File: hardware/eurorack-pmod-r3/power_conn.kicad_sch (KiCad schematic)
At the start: 24 parts, among them J1 CONN 2x5 P=2.54mm, J2 CONN 2x6 P=2.54mm

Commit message: Place everything on board, fix some bugs
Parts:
- removed C15, C5, C6: 47uF, Capacitor_SMD:CP_Elec_6.3x5.4, symbol Device:C_Polarized_Small
- added C13: 47.0uF, Capacitor_Tantalum_SMD:CP_EIA-3216-10_Kemet-I, symbol Device:C_Polarized_Small
- added J3: Conn_01x14_Socket, Connector_FFC-FPC:Hirose_FH12-14S-0.5SH_1x14-1MP_P0.50mm_Horizontal, symbol Connector:Conn_01x14_Socket
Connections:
- net BICK: now also J3.10 (Pin_10)
- net GND: now also J3.5 (Pin_5)
- net GNDD: now also C13.2, J3.6 (Pin_6)
- net LRCK: now also J3.9 (Pin_9)
- net MCLK: now also J3.11 (Pin_11)
- net PDN: now also J3.12 (Pin_12)
- net SCL: now also J3.14 (Pin_14)
- net SDA: now also J3.13 (Pin_13)
- net SDIN1: now also J3.7 (Pin_7)
- net SDOUT1: now also J3.8 (Pin_8)
- net VDD: now also C13.1
- net C_P12V: now reaches D1.1 (K), L1.2
- net C_P12V: now also J3.3 (Pin_3)
- net C_N12V: now reaches D2.2 (A), L2.2
- net C_N12V: now also J3.1 (Pin_1)
- no-connect marks 0 -> 2
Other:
- note added: "FFC INGRESS"
- note added: "[REMOVED] Daughterboard AUX"
- note removed: "[REMOVED] DAUGHTERBOARD AUX"
- moved on the sheet: D1, D2, J1, L1, L2

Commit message: Almost ready for layout
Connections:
- net +12V: now also J3.3 (Pin_3)
- net -12V: now also J3.1 (Pin_1)
- net GND: now also J3.4 (Pin_4); no longer J3.5 (Pin_5)
- net VDD: now also J3.5 (Pin_5)
- net C_N12V: no longer names the net of D2.2 (A), L2.2
- net C_N12V: no longer J3.1 (Pin_1)
- net C_P12V: no longer names the net of D1.1 (K), L1.2
- net C_P12V: no longer J3.3 (Pin_3)
- no-connect marks 2 -> 1
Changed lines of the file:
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@@
   (junction (at 45.72 88.9) (diameter 0) (color 0 0 0 0)
   )
-  (junction (at 50.038 43.18) (diameter 0) (color 0 0 0 0)
-  )
   (junction (at 96.012 30.099) (diameter 0) (color 0 0 0 0)
   )
@@
   (junction (at 25.4 38.1) (diameter 0) (color 0 0 0 0)
   )
-  (junction (at 50.038 33.02) (diameter 0) (color 0 0 0 0)
-  )
   (junction (at 77.089 50.292) (diameter 0) (color 0 0 0 0)
   )
@@
   (junction (at 102.235 94.615) (diameter 0) (color 0 0 0 0)
   )
-  (no_connect (at 148.844 46.228))
   (no_connect (at 148.844 41.148))
   (wire (pts (xy 75.184 45.212) (xy 77.089 45.212))
@@
     (stroke (width 0) (type default))
   )
-  (wire (pts (xy 50.038 43.18) (xy 52.705 43.18))
+  (wire (pts (xy 49.53 43.18) (xy 52.705 43.18))
     (stroke (width 0) (type default))
   )
@@
     (stroke (width 0) (type default))
   )
-  (wire (pts (xy 137.16 46.99) (xy 137.16 48.768))
-    (stroke (width 0) (type default))
-  )
   (wire (pts (xy 33.02 88.9) (xy 33.02 91.44))
     (stroke (width 0) (type default))
@@
     (stroke (width 0) (type default))
   )
-  (wire (pts (xy 49.53 33.02) (xy 50.038 33.02))
-    (stroke (width 0) (type default))
-  )
   (wire (pts (xy 136.144 51.308) (xy 148.844 51.308))
     (stroke (width 0) (type default))
@@
     (stroke (width 0) (type default))
   )
-  (wire (pts (xy 50.038 32.258) (xy 50.038 33.02))
-    (stroke (width 0) (type default))
-  )
   (wire (pts (xy 39.37 40.64) (xy 40.64 40.64))
     (stroke (width 0) (type default))
@@
     (stroke (width 0) (type default))
   )
-  (wire (pts (xy 50.038 42.418) (xy 50.038 43.18))
+  (wire (pts (xy 135.636 46.228) (xy 148.844 46.228))
     (stroke (width 0) (type default))
   )
@@
     (stroke (width 0) (type default))
   )
-  (wire (pts (xy 137.16 48.768) (xy 148.844 48.768))
-    (stroke (width 0) (type default))
-  )
   (wire (pts (xy 93.345 73.279) (xy 95.885 73.279))
     (stroke (width 0) (type default))
@@
     (stroke (width 0) (type default))
   )
-  (wire (pts (xy 50.038 33.02) (xy 52.705 33.02))
+  (wire (pts (xy 49.53 33.02) (xy 52.705 33.02))
     (stroke (width 0) (type default))
   )
@@
     (stroke (width 0) (type default))
   )
-  (wire (pts (xy 136.398 46.99) (xy 137.16 46.99))
-    (stroke (width 0) (type default))
-  )
   (wire (pts (xy 25.4 38.1) (xy 26.67 38.1))
     (stroke (width 0) (type default))
@@
     (stroke (width 0) (type default))
   )
-  (wire (pts (xy 49.53 43.18) (xy 50.038 43.18))
-    (stroke (width 0) (type default))
-  )
   (wire (pts (xy 40.64 35.56) (xy 40.64 38.1))
     (stroke (width 0) (type default))
@@
   )
   (polyline (pts (xy 113.03 128.905) (xy 16.51 128.905))
+    (stroke (width 0) (type default))
+  )
+  (wire (pts (xy 143.256 48.768) (xy 148.844 48.768))
     (stroke (width 0) (type default))
   )
@@
     (effects (font (size 1.27 1.27)) (justify left bottom))
   )
-  (label "C_N12V" (at 135.636 38.608 0) (fields_autoplaced)
-    (effects (font (size 1.27 1.27)) (justify left bottom))
-  )
   (label "C_SDOUT1" (at 24.13 78.74 0) (fields_autoplaced)
     (effects (font (size 1.27 1.27)) (justify left bottom))
@@
     (effects (font (size 1.27 1.27)) (justify left bottom))
   )
-  (label "C_P12V" (at 135.636 43.688 0) (fields_autoplaced)
-    (effects (font (size 1.27 1.27)) (justify left bottom))
-  )
   (label "C_SDIN1" (at 24.13 76.2 0) (fields_autoplaced)
     (effects (font (size 1.27 1.27)) (justify left bottom))
@@
     (effects (font (size 1.27 1.27)) (justify left bottom))
   )
-  (label "C_P12V" (at 50.038 32.258 0) (fields_autoplaced)
-    (effects (font (size 1.27 1.27)) (justify left bottom))
-  )
   (label "C_MCLK" (at 137.922 64.008 0) (fields_autoplaced)
     (effects (font (size 1.27 1.27)) (justify left bottom))
@@
   )
   (label "C_LRCK" (at 24.13 81.28 0) (fields_autoplaced)
-    (effects (font (size 1.27 1.27)) (justify left bottom))
-  )
-  (label "C_N12V" (at 50.038 42.418 0) (fields_autoplaced)
     (effects (font (size 1.27 1.27)) (justify left bottom))
   )
@@
     )
   )
-  (symbol (lib_id "power:GND") (at 136.398 46.99 270) (mirror x) (unit 1)
-    (in_bom yes) (on_board yes) (dnp no)
-    (property "Reference" "#PWR014" (at 130.048 46.99 0)
-      (effects (font (size 1.27 1.27)) hide)
-    )
-    (property "Value" "GND" (at 129.667 46.99 90)
+  (symbol (lib_id "power:GND") (at 135.636 46.228 270) (mirror x) (unit 1)
+    (in_bom yes) (on_board yes) (dnp no)
+    (property "Reference" "#PWR014" (at 129.286 46.228 0)
+      (effects (font (size 1.27 1.27)) hide)
+    )
+    (property "Value" "GND" (at 128.905 46.228 90)
       (effects (font (size 1.27 1.27)) (justify left))
     )
-    (property "Footprint" "" (at 136.398 46.99 0)
-      (effects (font (size 1.27 1.27)) hide)
-    )
-    (property "Datasheet" "" (at 136.398 46.99 0)
+    (property "Footprint" "" (at 135.636 46.228 0)
+      (effects (font (size 1.27 1.27)) hide)
+    )
+    (property "Datasheet" "" (at 135.636 46.228 0)
       (effects (font (size 1.27 1.27)) hide)
     )
@@
     )
   )
+  (symbol (lib_id "power:-12V") (at 135.636 38.608 90) (unit 1)
+    (in_bom yes) (on_board yes) (dnp no)
+    (property "Reference" "#PWR018" (at 133.096 38.608 0)
+      (effects (font (size 1.27 1.27)) hide)
+    )
+    (property "Value" "-12V" (at 132.588 38.608 90)
+      (effects (font (size 1.27 1.27)) (justify left))
+    )
+    (property "Footprint" "" (at 135.636 38.608 0)
+      (effects (font (size 1.27 1.27)) hide)
+    )
+    (property "Datasheet" "" (at 135.636 38.608 0)
+      (effects (font (size 1.27 1.27)) hide)
+    )
+    (pin "1")
+    (instances
+      (project "eurorack-pmod-pcb"
+        (path "/d1469efb-590b-4a61-a37b-5bbc286936ba"
+          (reference "#PWR018") (unit 1)
+        )
+        (path "/d1469efb-590b-4a61-a37b-5bbc286936ba/8bd0f3ad-78ad-46cf-a63b-58b9dbc835d8"
+          (reference "#PWR0115") (unit 1)
+        )
+      )
+    )
+  )
+  (symbol (lib_id "power:+12V") (at 135.636 43.688 90) (unit 1)
+    (in_bom yes) (on_board yes) (dnp no)
+    (property "Reference" "#PWR012" (at 139.446 43.688 0)
+      (effects (font (size 1.27 1.27)) hide)
+    )
+    (property "Value" "+12V" (at 127.254 43.688 90)
+      (effects (font (size 1.27 1.27)) (justify right))
+    )
+    (property "Footprint" "" (at 135.636 43.688 0)
+      (effects (font (size 1.27 1.27)) hide)
+    )
+    (property "Datasheet" "" (at 135.636 43.688 0)
+      (effects (font (size 1.27 1.27)) hide)
+    )
+    (pin "1")
+    (instances
+      (project "eurorack-pmod-pcb"
+        (path "/d1469efb-590b-4a61-a37b-5bbc286936ba"
+          (reference "#PWR012") (unit 1)
+        )
+        (path "/d1469efb-590b-4a61-a37b-5bbc286936ba/8bd0f3ad-78ad-46cf-a63b-58b9dbc835d8"
+          (reference "#PWR0114") (unit 1)
+        )
+      )
+    )
+  )
   (symbol (lib_id "Device:C_Polarized_Small") (at 93.98 113.665 0) (mirror y) (unit 1)
     (in_bom yes) (on_board yes) (dnp no)
@@
         )
       )
+    )
+  )
+  (symbol (lib_id "power:VDD") (at 143.256 48.768 90) (unit 1)
+    (in_bom yes) (on_board yes) (dnp no)
+    (property "Reference" "#PWR034" (at 147.066 48.768 0)
+      (effects (font (size 1.27 1.27)) hide)
+    )
+    (property "Value" "VDD" (at 137.922 48.768 90)
+      (effects (font (size 1.27 1.27)))
+    )
+    (property "Footprint" "" (at 143.256 48.768 0)
+      (effects (font (size 1.27 1.27)) hide)
+    )
+    (property "Datasheet" "" (at 143.256 48.768 0)
+      (effects (font (size 1.27 1.27)) hide)
+    )
+    (pin "1")
+    (instances
+      (project "eurorack-pmod-pcb"
+        (path "/d1469efb-590b-4a61-a37b-5bbc286936ba"
+          (reference "#PWR034") (unit 1)
+        )
+        (path "/d1469efb-590b-4a61-a37b-5bbc286936ba/8bd0f3ad-78ad-46cf-a63b-58b9dbc835d8"
+          (reference "#PWR0116") (unit 1)
+        )
+      )

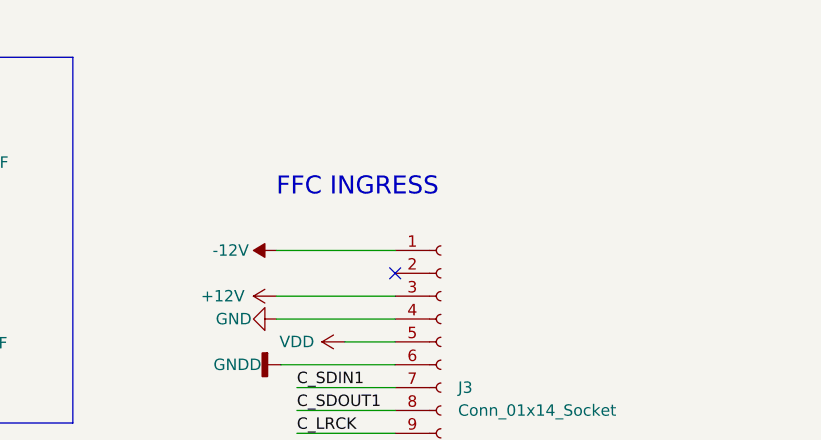
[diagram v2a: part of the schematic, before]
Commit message: add LCSC part numbers for every component to populate
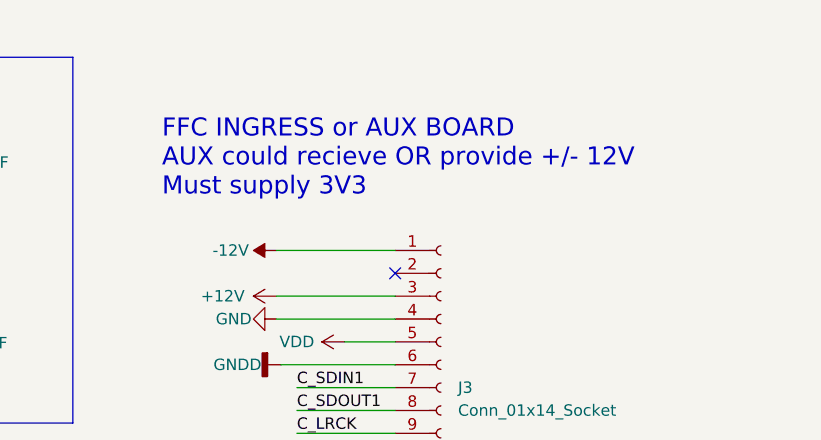
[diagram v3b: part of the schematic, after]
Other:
- note added: "FFC INGRESS or AUX BOARD AUX could recieve OR provide +/- 12V Must supply 3V3"
- note removed: "FFC INGRESS"
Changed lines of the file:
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@@
     (effects (font (size 2 2)) (justify left bottom))
   )
-  (text "FFC INGRESS" (at 135.636 32.766 0)
+  (text "FFC INGRESS or AUX BOARD\nAUX could recieve OR provide +/- 12V\nMust supply 3V3"
+    (at 122.936 32.766 0)
     (effects (font (size 2 2)) (justify left bottom))
   )
@@
       (effects (font (size 1.27 1.27)) hide)
     )
-    (property "Datasheet" "https://datasheet.lcsc.com/lcsc/1810252220_KEMET-T491A106K016AT_C110055.pdf" (at 93.98 113.665 0)
+    (property "Datasheet" "" (at 93.98 113.665 0)
       (effects (font (size 1.27 1.27)) hide)
     )
@@
       (effects (font (size 1.27 1.27)) hide)
     )
-    (property "Datasheet" "https://datasheet.lcsc.com/lcsc/1810252220_KEMET-T491A106K016AT_C110055.pdf" (at 67.31 98.425 0)
+    (property "Datasheet" "" (at 67.31 98.425 0)
       (effects (font (size 1.27 1.27)) hide)
     )
@@
       (effects (font (size 1.27 1.27)) hide)
     )
-    (property "Datasheet" "https://datasheet.lcsc.com/lcsc/1810252220_KEMET-T491A106K016AT_C110055.pdf" (at 100.33 97.155 0)
-      (effects (font (size 1.27 1.27)) hide)
-    )
+    (property "Datasheet" "" (at 100.33 97.155 0)
+      (effects (font (size 1.27 1.27)) hide)
+    )

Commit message: fab: add gerber/pnp for r3.2 sent 3 Oct 23
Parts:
- C1, C10, C3, C8: value 10.0uF -> 22.0uF; dig# 399-18019-1-ND -> (none); lcsc# C110055 -> C782264; mfg# T491A106K016AT -> CA45-A-16V-22uF-K
- C13, C16: value 47.0uF -> 100.0uF; lcsc# C118999 -> C27279; mfg# T491A476K006AT -> TLJA107M006R0800
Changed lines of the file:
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@@
       (effects (font (size 1.27 1.27)))
     )
-    (property "Value" "10.0uF" (at 90.297 27.559 0)
+    (property "Value" "22.0uF" (at 90.297 27.559 0)
       (effects (font (size 1.27 1.27)))
     )
@@
       (effects (font (size 1.27 1.27)) hide)
     )
-    (property "Datasheet" "https://datasheet.lcsc.com/lcsc/1810252220_KEMET-T491A106K016AT_C110055.pdf" (at 94.107 27.559 0)
-      (effects (font (size 1.27 1.27)) hide)
-    )
-    (property "dig#" "399-18019-1-ND" (at 91.567 35.179 0)
-      (effects (font (size 1.27 1.27)) hide)
-    )
-    (property "mfg#" "T491A106K016AT" (at 91.567 37.719 0)
-      (effects (font (size 1.27 1.27)) hide)
-    )
-    (property "lcsc#" "C110055" (at 94.107 27.559 0)
+    (property "Datasheet" "" (at 94.107 27.559 0)
+      (effects (font (size 1.27 1.27)) hide)
+    )
+    (property "dig#" "" (at 91.567 35.179 0)
+      (effects (font (size 1.27 1.27)) hide)
+    )
+    (property "mfg#" "CA45-A-16V-22uF-K" (at 91.567 37.719 0)
+      (effects (font (size 1.27 1.27)) hide)
+    )
+    (property "lcsc#" "C782264" (at 94.107 27.559 0)
       (effects (font (size 1.27 1.27)) hide)
     )
@@
       (effects (font (size 1.27 1.27)))
     )
-    (property "Value" "10.0uF" (at 90.17 47.625 0)
+    (property "Value" "22.0uF" (at 90.17 47.625 0)
       (effects (font (size 1.27 1.27)))
     )
@@
       (effects (font (size 1.27 1.27)) hide)
     )
-    (property "Datasheet" "https://datasheet.lcsc.com/lcsc/1810252220_KEMET-T491A106K016AT_C110055.pdf" (at 93.98 47.625 0)
-      (effects (font (size 1.27 1.27)) hide)
-    )
-    (property "dig#" "399-18019-1-ND" (at 91.44 55.245 0)
-      (effects (font (size 1.27 1.27)) hide)
-    )
-    (property "mfg#" "T491A106K016AT" (at 91.44 57.785 0)
-      (effects (font (size 1.27 1.27)) hide)
-    )
-    (property "lcsc#" "C110055" (at 93.98 47.625 0)
+    (property "Datasheet" "" (at 93.98 47.625 0)
+      (effects (font (size 1.27 1.27)) hide)
+    )
+    (property "dig#" "" (at 91.44 55.245 0)
+      (effects (font (size 1.27 1.27)) hide)
+    )
+    (property "mfg#" "CA45-A-16V-22uF-K" (at 91.44 57.785 0)
+      (effects (font (size 1.27 1.27)) hide)
+    )
+    (property "lcsc#" "C782264" (at 93.98 47.625 0)
       (effects (font (size 1.27 1.27)) hide)
     )
@@
       (effects (font (size 1.27 1.27)))
     )
-    (property "Value" "10.0uF" (at 71.501 27.559 0)
+    (property "Value" "22.0uF" (at 71.501 27.559 0)
       (effects (font (size 1.27 1.27)))
     )
@@
       (effects (font (size 1.27 1.27)) hide)
     )
-    (property "Datasheet" "https://datasheet.lcsc.com/lcsc/1810252220_KEMET-T491A106K016AT_C110055.pdf" (at 75.311 27.559 0)
-      (effects (font (size 1.27 1.27)) hide)
-    )
-    (property "dig#" "399-18019-1-ND" (at 72.771 35.179 0)
-      (effects (font (size 1.27 1.27)) hide)
-    )
-    (property "mfg#" "T491A106K016AT" (at 72.771 37.719 0)
-      (effects (font (size 1.27 1.27)) hide)
-    )
-    (property "lcsc#" "C110055" (at 75.311 27.559 0)
+    (property "Datasheet" "" (at 75.311 27.559 0)
+      (effects (font (size 1.27 1.27)) hide)
+    )
+    (property "dig#" "" (at 72.771 35.179 0)
+      (effects (font (size 1.27 1.27)) hide)
+    )
+    (property "mfg#" "CA45-A-16V-22uF-K" (at 72.771 37.719 0)
+      (effects (font (size 1.27 1.27)) hide)
+    )
+    (property "lcsc#" "C782264" (at 75.311 27.559 0)
       (effects (font (size 1.27 1.27)) hide)
     )
@@
       (effects (font (size 1.27 1.27)))
     )
-    (property "Value" "47.0uF" (at 88.9 113.665 0)
+    (property "Value" "100.0uF" (at 88.9 113.665 0)
       (effects (font (size 1.27 1.27)))
     )
@@
       (effects (font (size 1.27 1.27)) hide)
     )
-    (property "mfg#" "T491A476K006AT" (at 91.44 123.825 0)
-      (effects (font (size 1.27 1.27)) hide)
-    )
-    (property "lcsc#" "C118999" (at 93.98 113.665 0)
+    (property "mfg#" "TLJA107M006R0800" (at 91.44 123.825 0)
+      (effects (font (size 1.27 1.27)) hide)
+    )
+    (property "lcsc#" "C27279" (at 93.98 113.665 0)
       (effects (font (size 1.27 1.27)) hide)
     )
@@
       (effects (font (size 1.27 1.27)))
     )
-    (property "Value" "47.0uF" (at 62.23 98.425 0)
+    (property "Value" "100.0uF" (at 62.23 98.425 0)
       (effects (font (size 1.27 1.27)))
     )
@@
       (effects (font (size 1.27 1.27)) hide)
     )
-    (property "mfg#" "T491A476K006AT" (at 64.77 108.585 0)
-      (effects (font (size 1.27 1.27)) hide)
-    )
-    (property "lcsc#" "C118999" (at 67.31 98.425 0)
+    (property "mfg#" "TLJA107M006R0800" (at 64.77 108.585 0)
+      (effects (font (size 1.27 1.27)) hide)
+    )
+    (property "lcsc#" "C27279" (at 67.31 98.425 0)
       (effects (font (size 1.27 1.27)) hide)
     )
@@
       (effects (font (size 1.27 1.27)))
     )
-    (property "Value" "10.0uF" (at 71.374 47.752 0)
+    (property "Value" "22.0uF" (at 71.374 47.752 0)
       (effects (font (size 1.27 1.27)))
     )
@@
       (effects (font (size 1.27 1.27)) hide)
     )
-    (property "Datasheet" "https://datasheet.lcsc.com/lcsc/1810252220_KEMET-T491A106K016AT_C110055.pdf" (at 75.184 47.752 0)
-      (effects (font (size 1.27 1.27)) hide)
-    )
-    (property "dig#" "399-18019-1-ND" (at 72.644 55.372 0)
-      (effects (font (size 1.27 1.27)) hide)
-    )
-    (property "mfg#" "T491A106K016AT" (at 72.644 57.912 0)
-      (effects (font (size 1.27 1.27)) hide)
-    )
-    (property "lcsc#" "C110055" (at 75.184 47.752 0)
+    (property "Datasheet" "" (at 75.184 47.752 0)
+      (effects (font (size 1.27 1.27)) hide)
+    )
+    (property "dig#" "" (at 72.644 55.372 0)
+      (effects (font (size 1.27 1.27)) hide)
+    )
+    (property "mfg#" "CA45-A-16V-22uF-K" (at 72.644 57.912 0)
+      (effects (font (size 1.27 1.27)) hide)
+    )
+    (property "lcsc#" "C782264" (at 75.184 47.752 0)
       (effects (font (size 1.27 1.27)) hide)
     )
@@
       (effects (font (size 1.27 1.27)))
     )
-    (property "Value" "47.0uF" (at 95.25 97.155 0)
+    (property "Value" "100.0uF" (at 95.25 97.155 0)
       (effects (font (size 1.27 1.27)))
     )
@@
       (effects (font (size 1.27 1.27)) hide)
     )
-    (property "mfg#" "T491A476K006AT" (at 97.79 107.315 0)
-      (effects (font (size 1.27 1.27)) hide)
-    )
-    (property "lcsc#" "C118999" (at 100.33 97.155 0)
-      (effects (font (size 1.27 1.27)) hide)
-    )
+    (property "mfg#" "TLJA107M006R0800" (at 97.79 107.315 0)
+      (effects (font (size 1.27 1.27)) hide)
+    )
+    (property "lcsc#" "C27279" (at 100.33 97.155 0)
+      (effects (font (size 1.27 1.27)) hide)
+    )
